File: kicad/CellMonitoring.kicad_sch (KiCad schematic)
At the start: 55 parts, among them U1 HDC3022, U11 TMCS1123x3, U12 DAC7571, U13 DAC7571, U14 TMCS1123x3, U17 LTC6803-4, U20 LTC6803-4, U21 LTC6803-4, U3 HDC3022, U4 HDC3022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

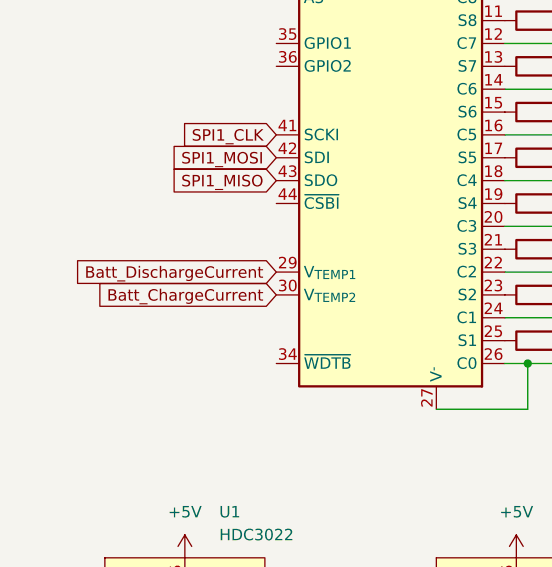
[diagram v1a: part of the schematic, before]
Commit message: Replaced STM32G0B1RBTx with STM32G0B1KCUx, simplified balancing control
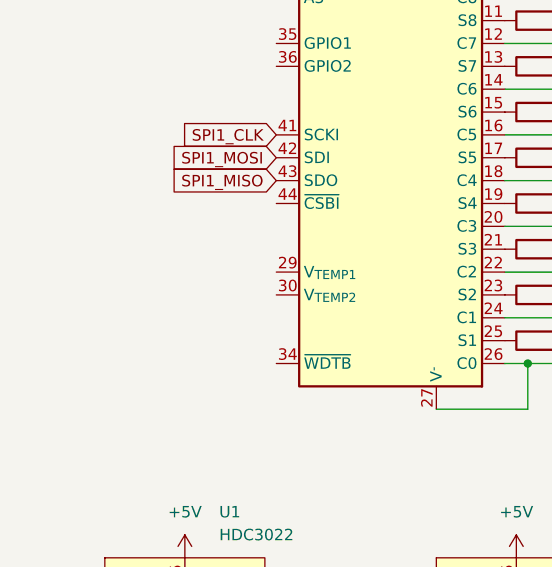
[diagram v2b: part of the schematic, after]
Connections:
- net Batt_DischargeCurrent: no longer U17.29 (V_{TEMP1})
- net Batt_ChargeCurrent: no longer names the net of U17.30 (V_{TEMP2})
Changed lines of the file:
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@@
-    )
-  )
-  (global_label "Batt_ChargeCurrent" (shape input) (at 49.53 81.28 180) (fields_autoplaced)
-    (effects (font (size 1.27 1.27)) (justify right))
-    (property "Intersheetrefs" "${INTERSHEET_REFS}" (at 28.1603 81.28 0)
-      (effects (font (size 1.27 1.27)) (justify right) hide)
     )
   )
@@
     )
   )
-  (global_label "Batt_DischargeCurrent" (shape input) (at 49.53 78.74 180) (fields_autoplaced)
-    (effects (font (size 1.27 1.27)) (justify right))
-    (property "Intersheetrefs" "${INTERSHEET_REFS}" (at 25.4388 78.74 0)
-      (effects (font (size 1.27 1.27)) (justify right) hide)
-    )
-  )

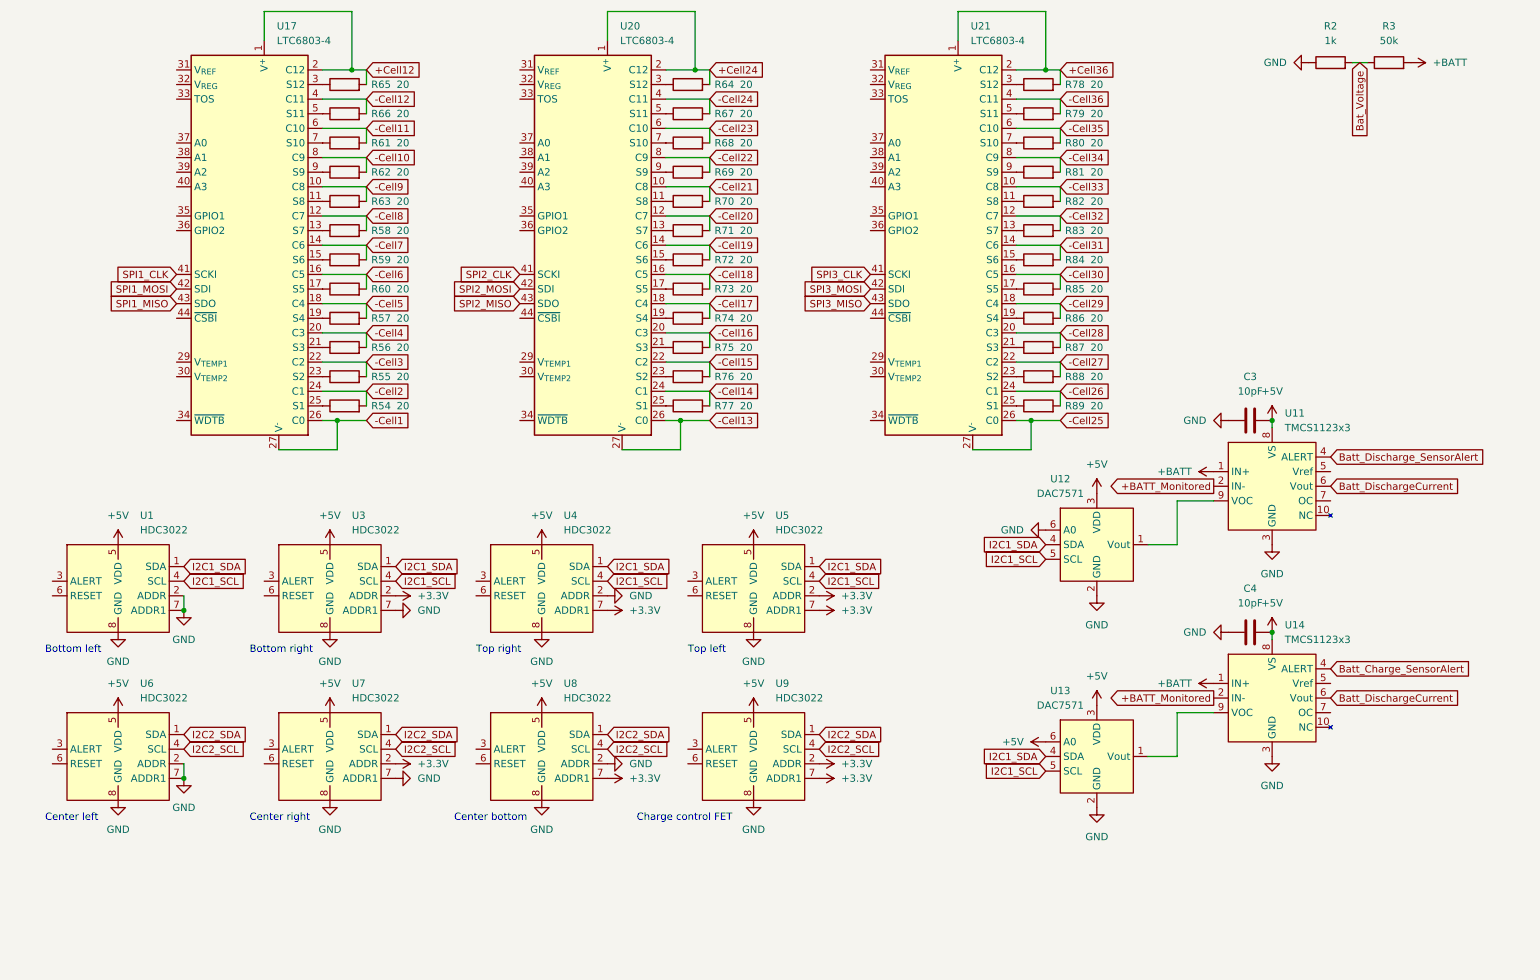
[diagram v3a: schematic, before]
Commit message: Started adding better temp sensors (SBMS-T-1)
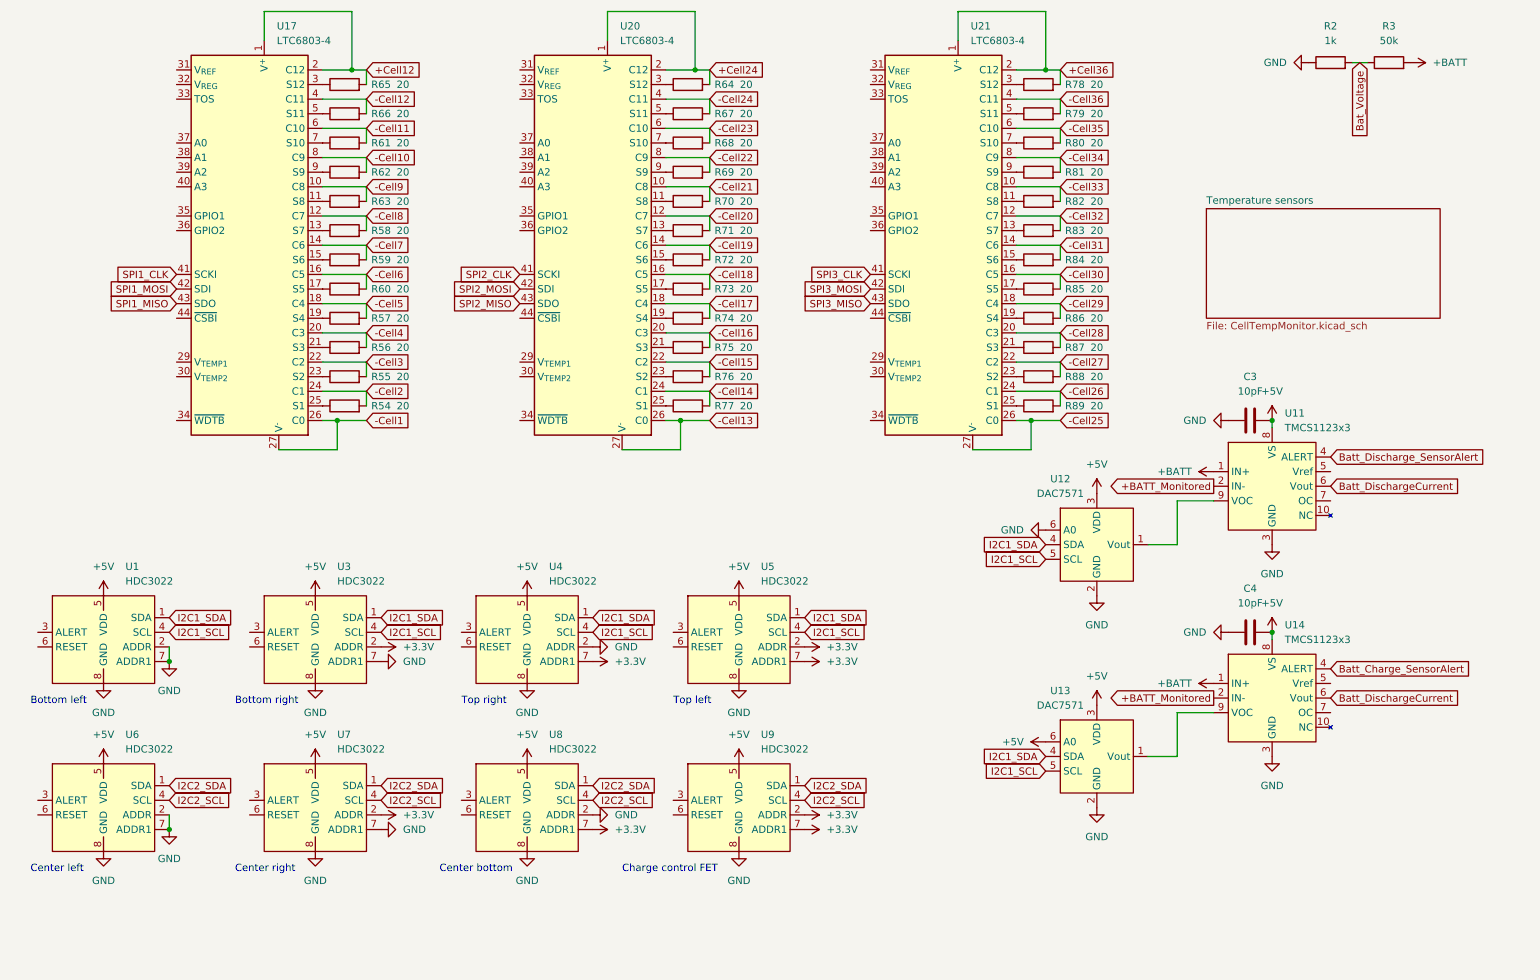
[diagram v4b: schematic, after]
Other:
- added sheet Temperature sensors (CellTempMonitor.kicad_sch)
- moved on the sheet: U1, U3, U4, U5, U6, U7, U8, U9

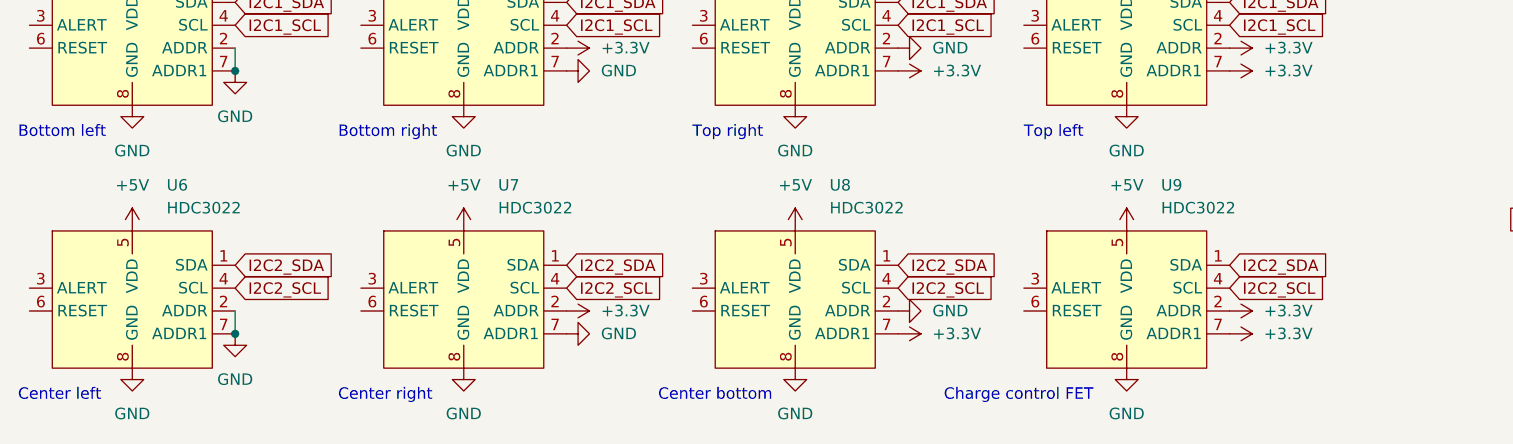
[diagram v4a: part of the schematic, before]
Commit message: removed center mounted humidity sensors (HDC302x)
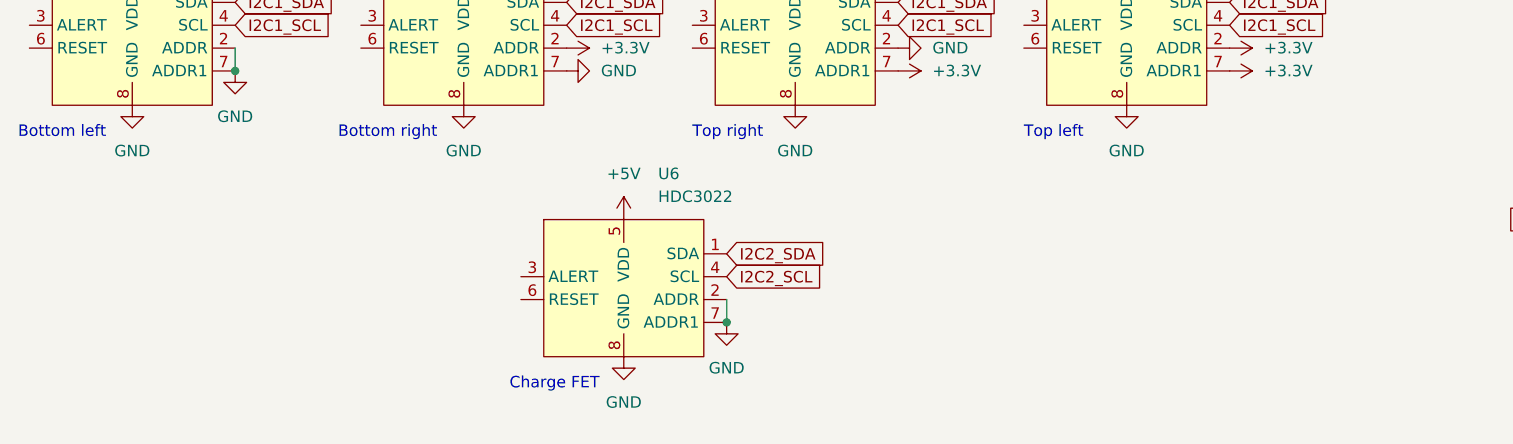
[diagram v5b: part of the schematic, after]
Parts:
- removed U7, U8, U9: HDC3022, Package_SON:Texas_S-PWSON-N8_EP1.2x2mm, symbol Sensor_Humidity:HDC3022
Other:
- note added: "Charge FET"
- note removed: "Center bottom"
- note removed: "Center left"
- note removed: "Center right"
- note removed: "Charge control FET"
- moved on the sheet: U6

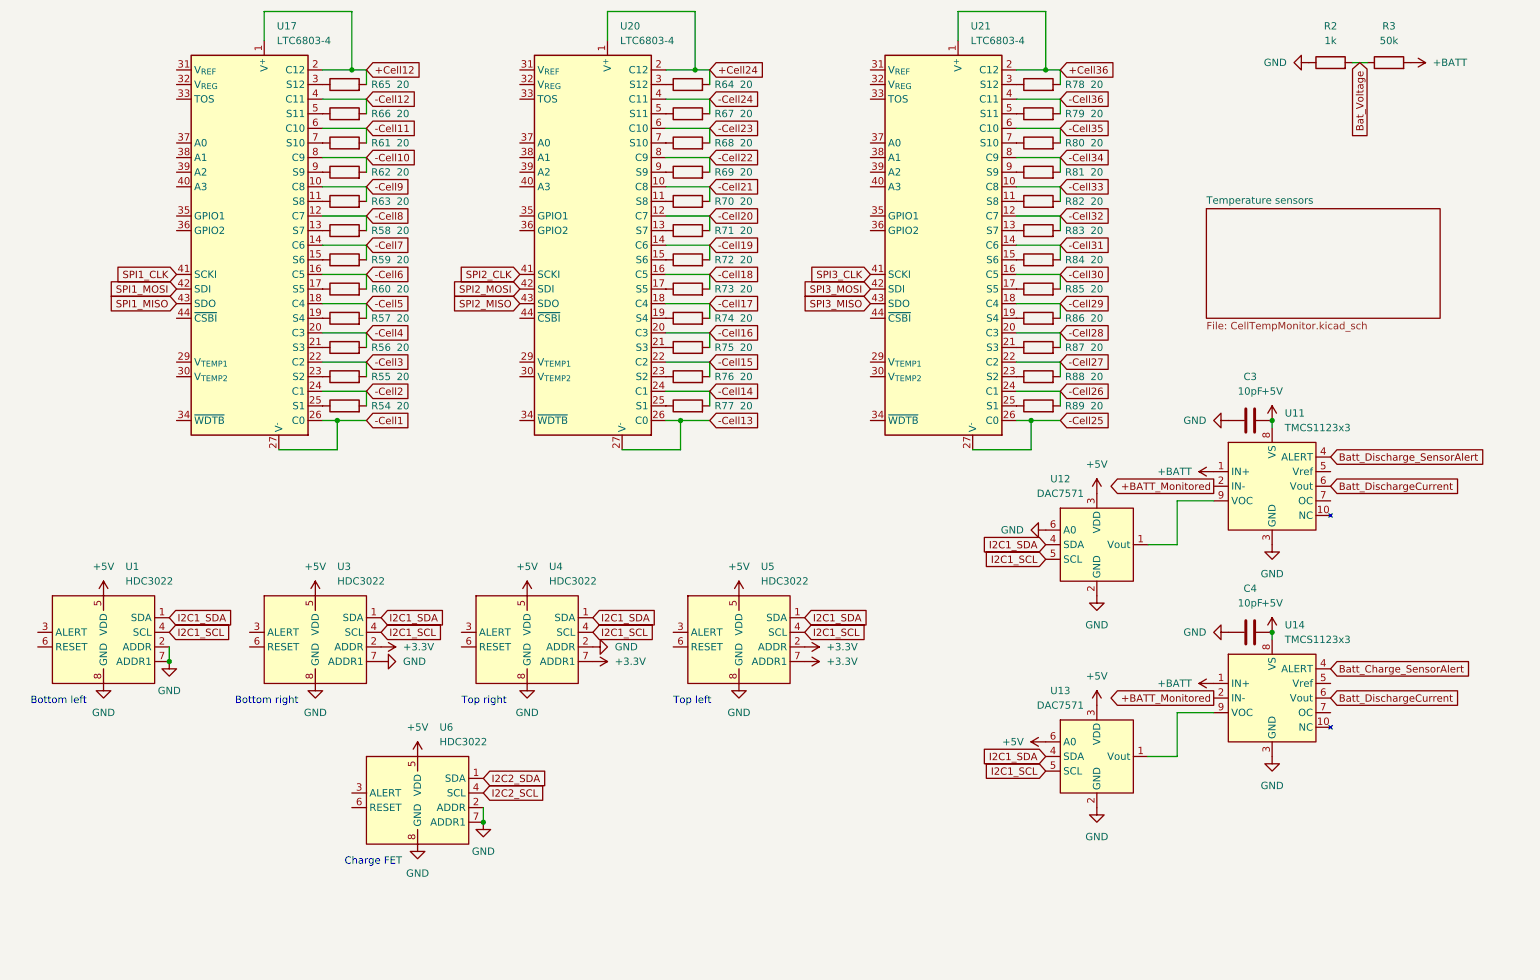
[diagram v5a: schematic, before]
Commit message: Added MLX90632 IR temperature sensor
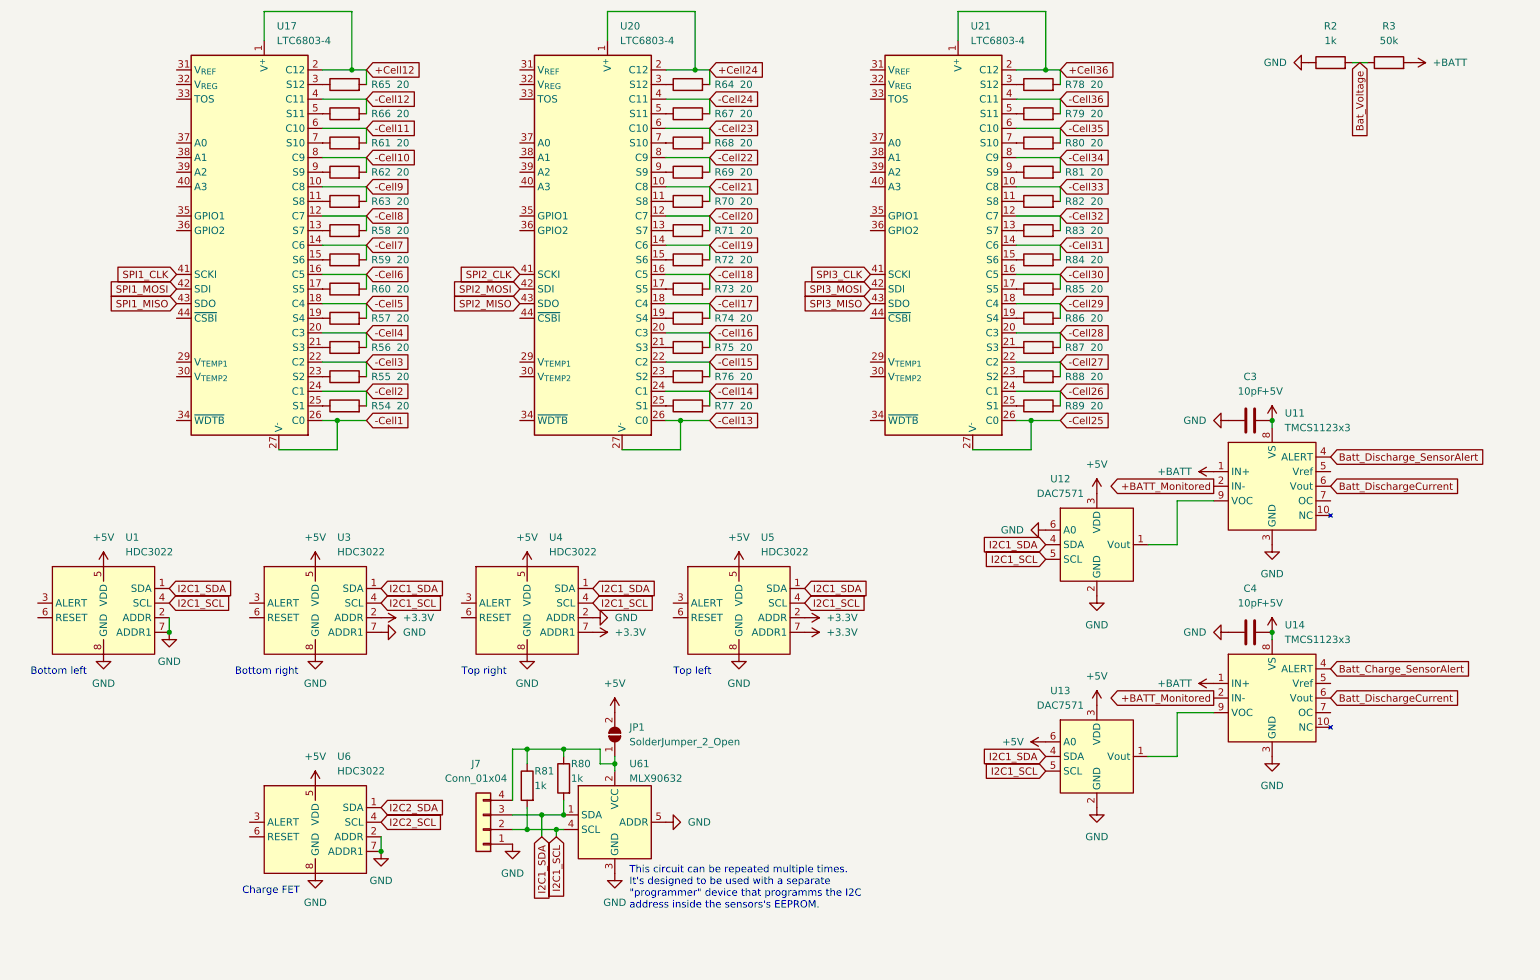
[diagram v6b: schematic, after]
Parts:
- added J7: Conn_01x04, symbol Connector_Generic:Conn_01x04
- added JP1: SolderJumper_2_Open, symbol Jumper:SolderJumper_2_Open
- added R80, R81: 1k, symbol Device:R
- added U61: MLX90632, symbol sBMS:MLX90632
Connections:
- net +5V: now also JP1.2 (B)
- net GND: now also J7.1 (Pin_1), U61.3 (GND), U61.5 (ADDR)
- net I2C1_SCL: now also J7.2 (Pin_2), R81.2, U61.4 (SCL)
- net I2C1_SDA: now also J7.3 (Pin_3), R80.2, U61.1 (SDA)
- new net: J7.4 (Pin_4), JP1.1 (A), R80.1, R81.1, U61.2 (VCC)
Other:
- removed sheet Temperature sensors
- note added: "This circuit can be repeated multiple times. It's designed to be used with a separate "programmer" device that programms the I2C address inside the sensors's EEPROM."
- moved on the sheet: U1, U3, U4, U5, U6
